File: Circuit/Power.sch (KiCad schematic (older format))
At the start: 16 parts, among them Q201 FDN340P, Q202 FDN340P, Q203 FDN340P, U201 CN3063, U202 MCP6002

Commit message: Add capacitor on VBAT, mitigate oscillation at end of charge
Because VBAT was otherwise disconnected when charging finished, the
voltage oscillated from charge/done/charge a lot.
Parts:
- added C204: 10uF 16V, FT:1210_CAP, symbol C
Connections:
- wire segments 54 -> 56
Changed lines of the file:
@@
 Charging current\nIr = 252mA max
 $Comp
-L GND #PWR204
+L GND #PWR205
 U 1 1 56417FB3
 P 7450 4100
-F 0 "#PWR204" H 7450 3850 50  0001 C CNN
+F 0 "#PWR205" H 7450 3850 50  0001 C CNN
 F 1 "GND" H 7450 3950 50  0000 C CNN
 F 2 "" H 7450 4100 60  0000 C CNN
@@
 VOUT
 $Comp
-L GND #PWR207
+L GND #PWR208
 U 1 1 5641AA9F
 P 10250 2500
-F 0 "#PWR207" H 10250 2250 50  0001 C CNN
+F 0 "#PWR208" H 10250 2250 50  0001 C CNN
 F 1 "GND" H 10250 2350 50  0000 C CNN
 F 2 "" H 10250 2500 60  0000 C CNN
@@
 VOUT
 $Comp
-L GND #PWR205
+L GND #PWR206
 U 1 1 5642C1C1
 P 9000 4100
-F 0 "#PWR205" H 9000 3850 50  0001 C CNN
+F 0 "#PWR206" H 9000 3850 50  0001 C CNN
 F 1 "GND" H 9000 3950 50  0000 C CNN
 F 2 "" H 9000 4100 60  0000 C CNN
@@
 $EndComp
 $Comp
-L GND #PWR206
+L GND #PWR207
 U 1 1 5642DA26
 P 10000 4150
-F 0 "#PWR206" H 10000 3900 50  0001 C CNN
+F 0 "#PWR207" H 10000 3900 50  0001 C CNN
 F 1 "GND" H 10000 4000 50  0000 C CNN
 F 2 "" H 10000 4150 60  0000 C CNN
@@
 	2450 3050 2950 3050
 Connection ~ 2700 3050
+$Comp
+L C C204
+U 1 1 566F9EBD
+P 6300 2850
+F 0 "C204" H 6325 2950 50  0000 L CNN
+F 1 "10uF 16V" H 6325 2750 50  0000 L CNN
+F 2 "FT:1210_CAP" H 6450 2700 24  0000 C CNN
+F 3 "" H 6300 2850 60  0000 C CNN
+	1    6300 2850
+	1    0    0    -1
+$EndComp
+Wire Wire Line
+	6300 2700 6300 2500
+Connection ~ 6300 2500
+Wire Wire Line
+	6300 3000 6300 3100
+$Comp
+L GND #PWR204
+U 1 1 566FA00B
+P 6300 3100
+F 0 "#PWR204" H 6300 2850 50  0001 C CNN
+F 1 "GND" H 6300 2950 50  0000 C CNN
+F 2 "" H 6300 3100 60  0000 C CNN
+F 3 "" H 6300 3100 60  0000 C CNN
+	1    6300 3100
+	1    0    0    -1
+$EndComp
 $EndSCHEMATC

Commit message: Add bulk capacitor on VBAT, mitigate oscillation at end of charge
Because VBAT was otherwise disconnected when charging finished meaning
with very low capacitance, the voltage oscillated from charge/done/charge.
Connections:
- wire segments 56 -> 55
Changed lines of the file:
@@
 	1    0    0    -1
 $EndComp
-Wire Wire Line
-	5400 2200 5400 1800
-Connection ~ 5400 1800
 $Comp
 L THERMISTOR TH201

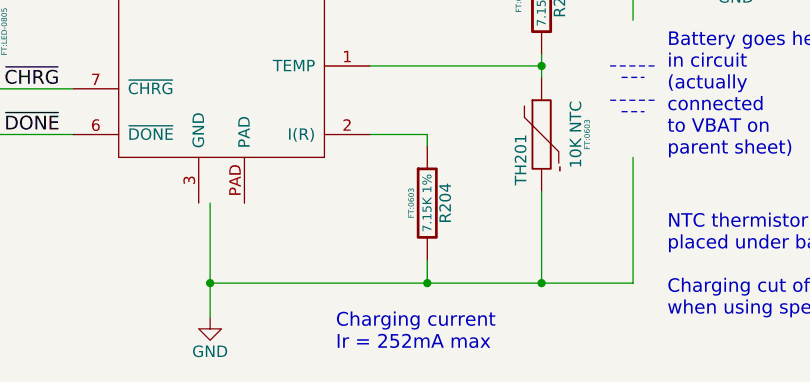
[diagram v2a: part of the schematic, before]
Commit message: Fix stray n/c trace, ground CN3063 pad, bump to V1.2
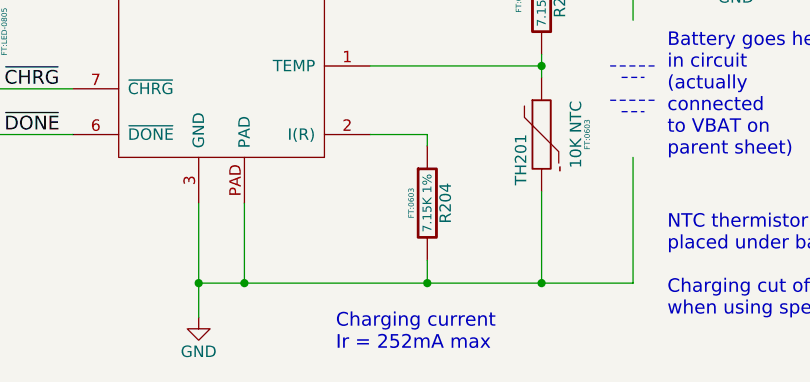
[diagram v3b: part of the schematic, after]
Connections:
- wire segments 55 -> 56
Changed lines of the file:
@@
 SOLAR_IN
 $Comp
-L GND #PWR202
+L GND #PWR033
 U 1 1 563C4E24
-P 4000 4650
-F 0 "#PWR202" H 4000 4400 50  0001 C CNN
-F 1 "GND" H 4000 4500 50  0000 C CNN
-F 2 "" H 4000 4650 60  0000 C CNN
-F 3 "" H 4000 4650 60  0000 C CNN
-	1    4000 4650
+P 3950 4650
+F 0 "#PWR033" H 3950 4400 50  0001 C CNN
+F 1 "GND" H 3950 4500 50  0000 C CNN
+F 2 "" H 3950 4650 60  0000 C CNN
+F 3 "" H 3950 4650 60  0000 C CNN
+	1    3950 4650
 	1    0    0    -1
 $EndComp
@@
 $EndComp
 $Comp
-L GND #PWR201
+L GND #PWR034
 U 1 1 563C5B2C
 P 1150 1500
-F 0 "#PWR201" H 1150 1250 50  0001 C CNN
+F 0 "#PWR034" H 1150 1250 50  0001 C CNN
 F 1 "GND" H 1150 1350 50  0000 C CNN
 F 2 "" H 1150 1500 60  0000 C CNN
@@
 Charging current\nIr = 252mA max
 $Comp
-L GND #PWR205
+L GND #PWR035
 U 1 1 56417FB3
 P 7450 4100
-F 0 "#PWR205" H 7450 3850 50  0001 C CNN
+F 0 "#PWR035" H 7450 3850 50  0001 C CNN
 F 1 "GND" H 7450 3950 50  0000 C CNN
 F 2 "" H 7450 4100 60  0000 C CNN
@@
 VOUT
 $Comp
-L GND #PWR208
+L GND #PWR036
 U 1 1 5641AA9F
 P 10250 2500
-F 0 "#PWR208" H 10250 2250 50  0001 C CNN
+F 0 "#PWR036" H 10250 2250 50  0001 C CNN
 F 1 "GND" H 10250 2350 50  0000 C CNN
 F 2 "" H 10250 2500 60  0000 C CNN
@@
 VOUT
 $Comp
-L GND #PWR206
+L GND #PWR037
 U 1 1 5642C1C1
 P 9000 4100
-F 0 "#PWR206" H 9000 3850 50  0001 C CNN
+F 0 "#PWR037" H 9000 3850 50  0001 C CNN
 F 1 "GND" H 9000 3950 50  0000 C CNN
 F 2 "" H 9000 4100 60  0000 C CNN
@@
 $EndComp
 $Comp
-L PWR_FLAG #FLG202
+L PWR_FLAG #FLG038
 U 1 1 5642D1CE
 P 10450 1800
-F 0 "#FLG202" H 10450 1895 50  0001 C CNN
+F 0 "#FLG038" H 10450 1895 50  0001 C CNN
 F 1 "PWR_FLAG" H 10450 1980 50  0000 C CNN
 F 2 "" H 10450 1800 60  0000 C CNN
@@
 $EndComp
 $Comp
-L PWR_FLAG #FLG201
+L PWR_FLAG #FLG039
 U 1 1 5642D5A3
 P 3900 1800
-F 0 "#FLG201" H 3900 1895 50  0001 C CNN
+F 0 "#FLG039" H 3900 1895 50  0001 C CNN
 F 1 "PWR_FLAG" H 3900 1980 50  0000 C CNN
 F 2 "" H 3900 1800 60  0000 C CNN
@@
 $EndComp
 $Comp
-L GND #PWR207
+L GND #PWR040
 U 1 1 5642DA26
 P 10000 4150
-F 0 "#PWR207" H 10000 3900 50  0001 C CNN
+F 0 "#PWR040" H 10000 3900 50  0001 C CNN
 F 1 "GND" H 10000 4000 50  0000 C CNN
 F 2 "" H 10000 4150 60  0000 C CNN
@@
 $EndComp
 $Comp
-L GND #PWR203
+L GND #PWR041
 U 1 1 5642CE9D
 P 4600 2350
-F 0 "#PWR203" H 4600 2100 50  0001 C CNN
+F 0 "#PWR041" H 4600 2100 50  0001 C CNN
 F 1 "GND" H 4600 2200 50  0000 C CNN
 F 2 "" H 4600 2350 60  0000 C CNN
@@
 	4700 3550 5450 3550
 Wire Wire Line
-	4000 4150 4000 4650
-Wire Wire Line
 	4950 3900 4950 3850
 Wire Wire Line
@@
 Wire Wire Line
 	2450 3600 2450 3850
-Wire Wire Line
-	4000 4500 5850 4500
-Connection ~ 4000 4500
 Wire Wire Line
 	4950 4400 4950 4500
@@
 	6300 3000 6300 3100
 $Comp
-L GND #PWR204
+L GND #PWR042
 U 1 1 566FA00B
 P 6300 3100
-F 0 "#PWR204" H 6300 2850 50  0001 C CNN
+F 0 "#PWR042" H 6300 2850 50  0001 C CNN
 F 1 "GND" H 6300 2950 50  0000 C CNN
 F 2 "" H 6300 3100 60  0000 C CNN
@@
 	1    0    0    -1
 $EndComp
+Wire Wire Line
+	3950 4500 5850 4500
+Wire Wire Line
+	3950 4150 3950 4650
+Wire Wire Line
+	4150 4500 4150 4150
+Connection ~ 4150 4500
+Connection ~ 3950 4500
 $EndSCHEMATC

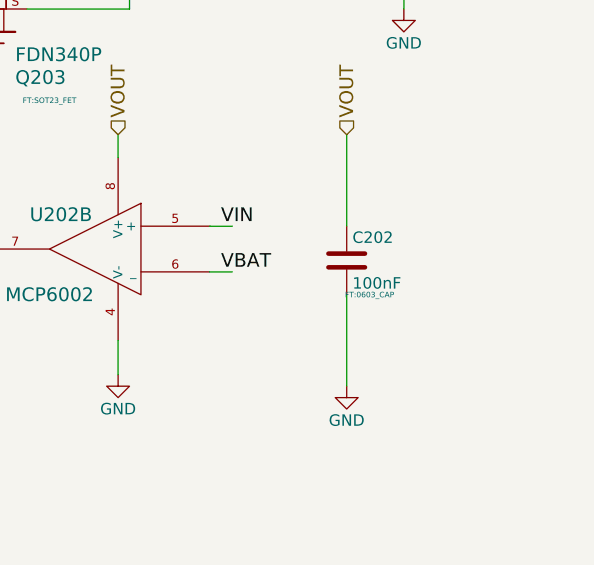
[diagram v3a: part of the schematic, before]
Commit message: Fix silkscreen & slot width issues noted by @hackvana, bump version V1.3
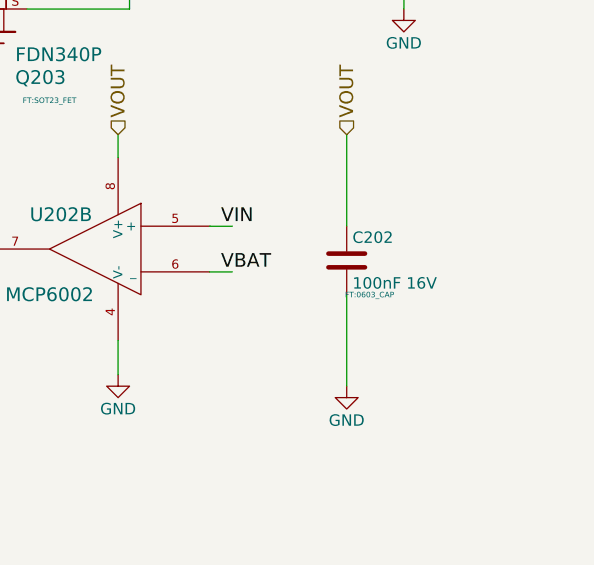
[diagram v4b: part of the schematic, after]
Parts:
- C202: value 100nF -> 100nF 16V
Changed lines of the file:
@@
 P 10000 3600
 F 0 "C202" H 10025 3700 50  0000 L CNN
-F 1 "100nF" H 10025 3500 50  0000 L CNN
+F 1 "100nF 16V" H 10025 3500 50  0000 L CNN
 F 2 "FT:0603_CAP" H 10100 3450 24  0000 C CNN
 F 3 "" H 10000 3600 60  0000 C CNN
